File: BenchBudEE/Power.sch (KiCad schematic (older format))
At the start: 11 parts

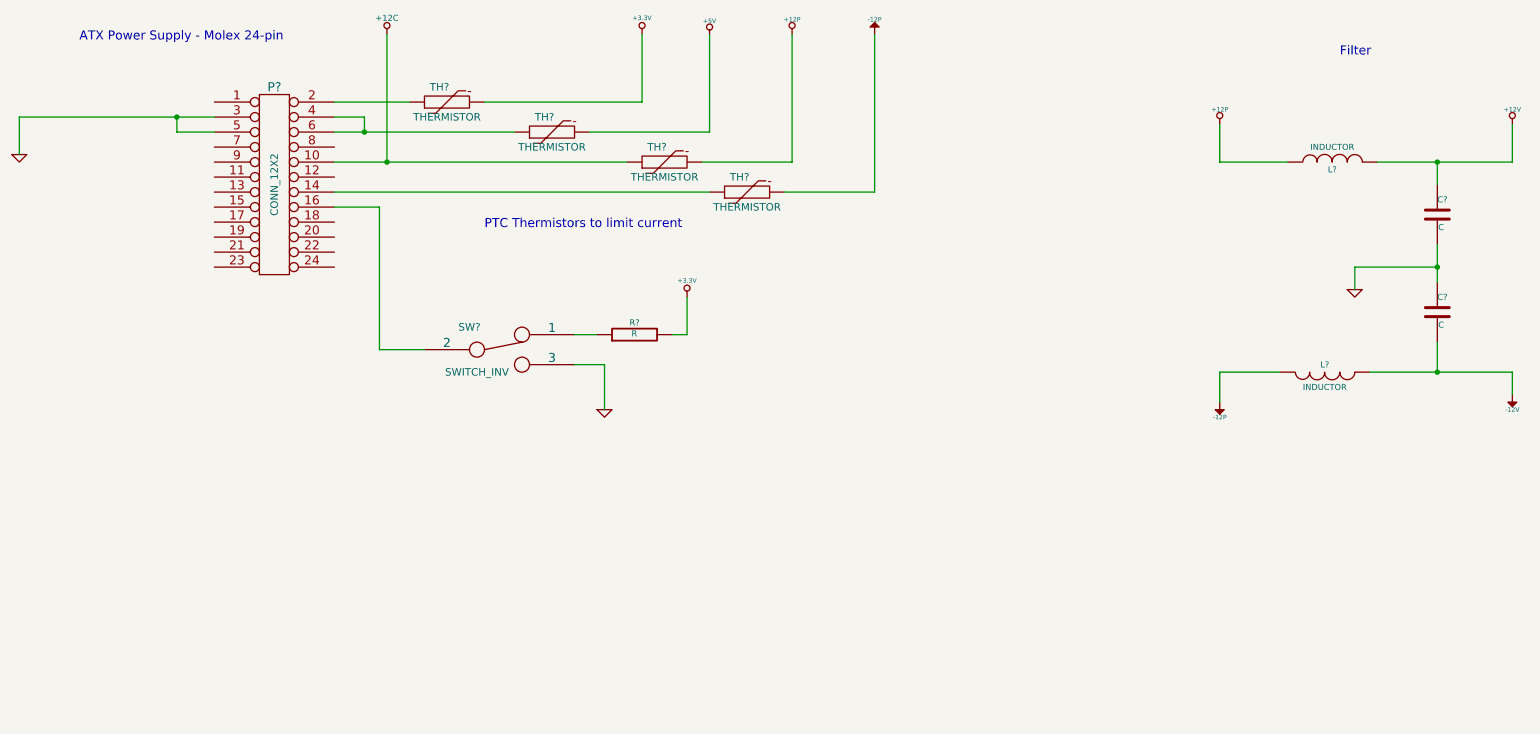
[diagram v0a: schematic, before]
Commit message: Connected Arduino power/ground. +5V power filtering. Removed current monitoring.
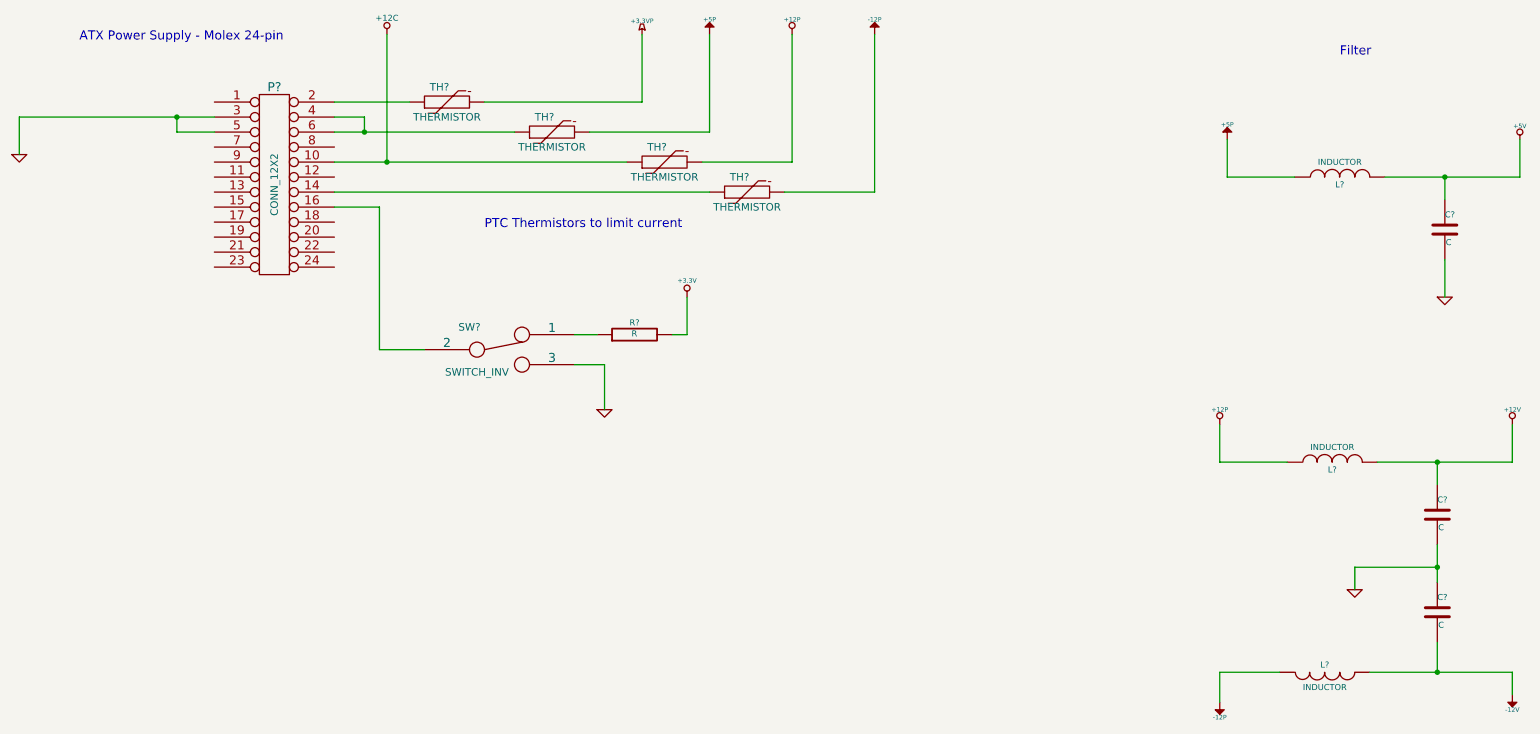
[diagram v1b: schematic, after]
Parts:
- added C?: C, ~, symbol C
- added L?: INDUCTOR, ~, symbol INDUCTOR
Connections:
- net +3.3V: no longer TH?.2
- net +5V: now also C?.1, L?.2; no longer TH?.2
- net GND: now also C?.2
- new net +3.3VP: TH?.2
- new net +5P: L?.1, TH?.2
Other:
- moved on the sheet: C?, L?
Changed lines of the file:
@@
 Sheet 4 9
 Title ""
-Date "14 feb 2014"
+Date "19 feb 2014"
 Rev ""
 Comp ""
@@
 Connection ~ 3150 1700
 Wire Wire Line
-	2150 1600 850  1600
+	850  1600 2150 1600
 Wire Wire Line
 	2150 1700 1900 1700
@@
 Text Notes 1250 1100 0    60   ~ 0
 ATX Power Supply - Molex 24-pin
-Connection ~ 10300 1900
-Wire Wire Line
-	10800 1900 10800 1650
+Connection ~ 10300 3900
+Wire Wire Line
+	10800 3900 10800 3650
 $Comp
 L +12V #PWR?
 U 1 1 52F6355D
-P 10800 1650
-F 0 "#PWR?" H 10800 1600 20  0001 C CNN
-F 1 "+12V" H 10800 1750 30  0000 C CNN
-F 2 "" H 10800 1650 60  0000 C CNN
-F 3 "" H 10800 1650 60  0000 C CNN
-	1    10800 1650
-	1    0    0    -1
-$EndComp
-Connection ~ 10300 3300
-Wire Wire Line
-	10800 3300 10800 3450
+P 10800 3650
+F 0 "#PWR?" H 10800 3600 20  0001 C CNN
+F 1 "+12V" H 10800 3750 30  0000 C CNN
+F 2 "" H 10800 3650 60  0000 C CNN
+F 3 "" H 10800 3650 60  0000 C CNN
+	1    10800 3650
+	1    0    0    -1
+$EndComp
+Connection ~ 10300 5300
+Wire Wire Line
+	10800 5300 10800 5450
 $Comp
 L -12V #PWR?
 U 1 1 52F63518
-P 10800 3450
-F 0 "#PWR?" H 10800 3580 20  0001 C CNN
-F 1 "-12V" H 10800 3550 30  0000 C CNN
-F 2 "" H 10800 3450 60  0000 C CNN
-F 3 "" H 10800 3450 60  0000 C CNN
-	1    10800 3450
+P 10800 5450
+F 0 "#PWR?" H 10800 5580 20  0001 C CNN
+F 1 "-12V" H 10800 5550 30  0000 C CNN
+F 2 "" H 10800 5450 60  0000 C CNN
+F 3 "" H 10800 5450 60  0000 C CNN
+	1    10800 5450
 	1    0    0    1
 $EndComp
-Connection ~ 10300 2600
-Wire Wire Line
-	9750 2600 10300 2600
-Wire Wire Line
-	9750 2750 9750 2600
-Wire Wire Line
-	8850 1900 8850 1650
-Wire Wire Line
-	9300 1900 8850 1900
-Wire Wire Line
-	9900 1900 10800 1900
-Wire Wire Line
-	10300 2050 10300 1900
-Wire Wire Line
-	10300 2700 10300 2450
-Wire Wire Line
-	10300 3300 10300 3100
-Wire Wire Line
-	9850 3300 10800 3300
-Wire Wire Line
-	8850 3300 9250 3300
-Wire Wire Line
-	8850 3500 8850 3300
+Connection ~ 10300 4600
+Wire Wire Line
+	9750 4600 10300 4600
+Wire Wire Line
+	9750 4750 9750 4600
+Wire Wire Line
+	8850 3900 8850 3650
+Wire Wire Line
+	9300 3900 8850 3900
+Wire Wire Line
+	9900 3900 10800 3900
+Wire Wire Line
+	10300 4050 10300 3900
+Wire Wire Line
+	10300 4450 10300 4700
+Wire Wire Line
+	10300 5300 10300 5100
+Wire Wire Line
+	9850 5300 10800 5300
+Wire Wire Line
+	8850 5300 9250 5300
+Wire Wire Line
+	8850 5500 8850 5300
 $Comp
 L C C?
 U 1 1 52F6342F
-P 10300 2250
-F 0 "C?" H 10300 2350 40  0000 L CNN
-F 1 "C" H 10306 2165 40  0000 L CNN
-F 2 "~" H 10338 2100 30  0000 C CNN
-F 3 "~" H 10300 2250 60  0000 C CNN
-	1    10300 2250
+P 10300 4250
+F 0 "C?" H 10300 4350 40  0000 L CNN
+F 1 "C" H 10306 4165 40  0000 L CNN
+F 2 "~" H 10338 4100 30  0000 C CNN
+F 3 "~" H 10300 4250 60  0000 C CNN
+	1    10300 4250
 	1    0    0    -1
 $EndComp
@@
 L C C?
 U 1 1 52F63418
-P 10300 2900
-F 0 "C?" H 10300 3000 40  0000 L CNN
-F 1 "C" H 10306 2815 40  0000 L CNN
-F 2 "~" H 10338 2750 30  0000 C CNN
-F 3 "~" H 10300 2900 60  0000 C CNN
-	1    10300 2900
+P 10300 4900
+F 0 "C?" H 10300 5000 40  0000 L CNN
+F 1 "C" H 10306 4815 40  0000 L CNN
+F 2 "~" H 10338 4750 30  0000 C CNN
+F 3 "~" H 10300 4900 60  0000 C CNN
+	1    10300 4900
 	1    0    0    -1
 $EndComp
@@
 L INDUCTOR L?
 U 1 1 52F63410
-P 9550 3300
-F 0 "L?" V 9500 3300 40  0000 C CNN
-F 1 "INDUCTOR" V 9650 3300 40  0000 C CNN
-F 2 "~" H 9550 3300 60  0000 C CNN
-F 3 "~" H 9550 3300 60  0000 C CNN
-	1    9550 3300
+P 9550 5300
+F 0 "L?" V 9500 5300 40  0000 C CNN
+F 1 "INDUCTOR" V 9650 5300 40  0000 C CNN
+F 2 "~" H 9550 5300 60  0000 C CNN
+F 3 "~" H 9550 5300 60  0000 C CNN
+	1    9550 5300
 	0    -1   1    0
 $EndComp
@@
 L INDUCTOR L?
 U 1 1 52F633F9
-P 9600 1900
-F 0 "L?" V 9550 1900 40  0000 C CNN
-F 1 "INDUCTOR" V 9700 1900 40  0000 C CNN
-F 2 "~" H 9600 1900 60  0000 C CNN
-F 3 "~" H 9600 1900 60  0000 C CNN
-	1    9600 1900
+P 9600 3900
+F 0 "L?" V 9550 3900 40  0000 C CNN
+F 1 "INDUCTOR" V 9700 3900 40  0000 C CNN
+F 2 "~" H 9600 3900 60  0000 C CNN
+F 3 "~" H 9600 3900 60  0000 C CNN
+	1    9600 3900
 	0    -1   -1   0
 $EndComp
@@
 L GND #PWR?
 U 1 1 52F633F1
-P 9750 2750
-F 0 "#PWR?" H 9750 2750 30  0001 C CNN
-F 1 "GND" H 9750 2680 30  0001 C CNN
-F 2 "" H 9750 2750 60  0000 C CNN
-F 3 "" H 9750 2750 60  0000 C CNN
-	1    9750 2750
+P 9750 4750
+F 0 "#PWR?" H 9750 4750 30  0001 C CNN
+F 1 "GND" H 9750 4680 30  0001 C CNN
+F 2 "" H 9750 4750 60  0000 C CNN
+F 3 "" H 9750 4750 60  0000 C CNN
+	1    9750 4750
 	1    0    0    -1
 $EndComp
@@
 L -12P #PWR?
 U 1 1 52F633EB
-P 8850 3500
-F 0 "#PWR?" H 8850 3630 20  0001 C CNN
-F 1 "-12P" H 8850 3600 30  0000 C CNN
-F 2 "" H 8850 3500 60  0000 C CNN
-F 3 "" H 8850 3500 60  0000 C CNN
-	1    8850 3500
+P 8850 5500
+F 0 "#PWR?" H 8850 5630 20  0001 C CNN
+F 1 "-12P" H 8850 5600 30  0000 C CNN
+F 2 "" H 8850 5500 60  0000 C CNN
+F 3 "" H 8850 5500 60  0000 C CNN
+	1    8850 5500
 	1    0    0    1
 $EndComp
@@
 L +12P #PWR?
 U 1 1 52F633E5
-P 8850 1650
-F 0 "#PWR?" H 8850 1620 30  0001 C CNN
-F 1 "+12P" H 8850 1750 30  0000 C CNN
-F 2 "" H 8850 1650 60  0000 C CNN
-F 3 "" H 8850 1650 60  0000 C CNN
-	1    8850 1650
+P 8850 3650
+F 0 "#PWR?" H 8850 3620 30  0001 C CNN
+F 1 "+12P" H 8850 3750 30  0000 C CNN
+F 2 "" H 8850 3650 60  0000 C CNN
+F 3 "" H 8850 3650 60  0000 C CNN
+	1    8850 3650
 	1    0    0    -1
 $EndComp
@@
 	1    0    0    -1
 $EndComp
-$Comp
-L +5V #PWR?
-U 1 1 52F62810
-P 5450 1050
-F 0 "#PWR?" H 5450 1140 20  0001 C CNN
-F 1 "+5V" H 5450 1140 30  0000 C CNN
-F 2 "" H 5450 1050 60  0000 C CNN
-F 3 "" H 5450 1050 60  0000 C CNN
-	1    5450 1050
-	1    0    0    -1
-$EndComp
-$Comp
-L +3.3V #PWR?
-U 1 1 52F627FA
-P 5000 1050
-F 0 "#PWR?" H 5000 1010 30  0001 C CNN
-F 1 "+3.3V" H 5000 1160 30  0000 C CNN
-F 2 "" H 5000 1050 60  0000 C CNN
-F 3 "" H 5000 1050 60  0000 C CNN
-	1    5000 1050
-	1    0    0    -1
-$EndComp
 Wire Wire Line
 	3300 1900 3300 1050
@@
 	0    -1   -1   0
 $EndComp
+Connection ~ 10350 2000
+Wire Wire Line
+	10850 2000 10850 1750
+Wire Wire Line
+	8900 2000 8900 1750
+Wire Wire Line
+	9350 2000 8900 2000
+Wire Wire Line
+	9950 2000 10850 2000
+Wire Wire Line
+	10350 2150 10350 2000
+$Comp
+L C C?
+U 1 1 53041CC8
+P 10350 2350
+F 0 "C?" H 10350 2450 40  0000 L CNN
+F 1 "C" H 10356 2265 40  0000 L CNN
+F 2 "~" H 10388 2200 30  0000 C CNN
+F 3 "~" H 10350 2350 60  0000 C CNN
+	1    10350 2350
+	1    0    0    -1
+$EndComp
+$Comp
+L INDUCTOR L?
+U 1 1 53041CCE
+P 9650 2000
+F 0 "L?" V 9600 2000 40  0000 C CNN
+F 1 "INDUCTOR" V 9750 2000 40  0000 C CNN
+F 2 "~" H 9650 2000 60  0000 C CNN
+F 3 "~" H 9650 2000 60  0000 C CNN
+	1    9650 2000
+	0    -1   -1   0
+$EndComp
+Wire Wire Line
+	10350 2550 10350 2800
+$Comp
+L GND #PWR?
+U 1 1 53041D20
+P 10350 2800
+F 0 "#PWR?" H 10350 2800 30  0001 C CNN
+F 1 "GND" H 10350 2730 30  0001 C CNN
+F 2 "" H 10350 2800 60  0000 C CNN
+F 3 "" H 10350 2800 60  0000 C CNN
+	1    10350 2800
+	1    0    0    -1
+$EndComp
+$Comp
+L +5P #PWR?
+U 1 1 53041F77
+P 5450 1050
+F 0 "#PWR?" H 5450 1180 20  0001 C CNN
+F 1 "+5P" H 5450 1150 30  0000 C CNN
+F 2 "" H 5450 1050 60  0000 C CNN
+F 3 "" H 5450 1050 60  0000 C CNN
+	1    5450 1050
+	1    0    0    -1
+$EndComp
+$Comp
+L +5P #PWR?
+U 1 1 53041F84
+P 8900 1750
+F 0 "#PWR?" H 8900 1880 20  0001 C CNN
+F 1 "+5P" H 8900 1850 30  0000 C CNN
+F 2 "" H 8900 1750 60  0000 C CNN
+F 3 "" H 8900 1750 60  0000 C CNN
+	1    8900 1750
+	1    0    0    -1
+$EndComp
+$Comp
+L +3.3VP #PWR?
+U 1 1 530421E7
+P 5000 1050
+F 0 "#PWR?" H 5050 1080 20  0001 C CNN
+F 1 "+3.3VP" H 5000 1140 30  0000 C CNN
+F 2 "" H 5000 1050 60  0000 C CNN
+F 3 "" H 5000 1050 60  0000 C CNN
+	1    5000 1050
+	1    0    0    -1
+$EndComp
+$Comp
+L +5V #PWR?
+U 1 1 530426C4
+P 10850 1750
+F 0 "#PWR?" H 10850 1840 20  0001 C CNN
+F 1 "+5V" H 10850 1840 30  0000 C CNN
+F 2 "" H 10850 1750 60  0000 C CNN
+F 3 "" H 10850 1750 60  0000 C CNN
+	1    10850 1750
+	1    0    0    -1
+$EndComp
 $EndSCHEMATC

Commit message: Placed the relay components.
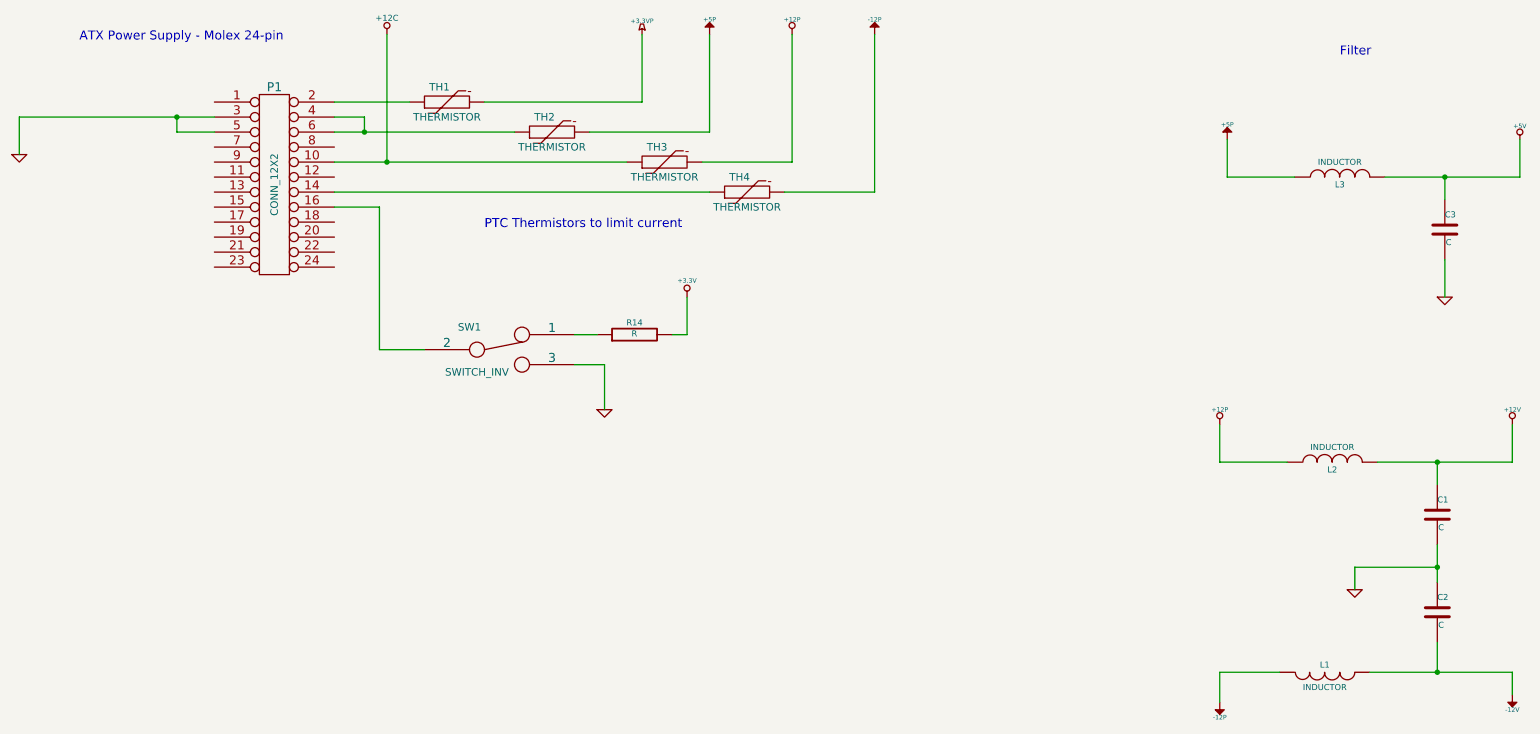
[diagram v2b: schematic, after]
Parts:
- gave numbers to parts that had none: 13
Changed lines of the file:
@@
 Sheet 4 9
 Title ""
-Date "19 feb 2014"
+Date "20 feb 2014"
 Rev ""
 Comp ""
@@
 $EndDescr
 $Comp
-L CONN_12X2 P?
+L CONN_12X2 P1
 U 1 1 52F627D0
 P 2550 2050
-F 0 "P?" H 2550 2700 60  0000 C CNN
+F 0 "P1" H 2550 2700 60  0000 C CNN
 F 1 "CONN_12X2" V 2550 2050 50  0000 C CNN
 F 2 "" H 2550 2050 60  0000 C CNN
@@
 	850  1600 850  1850
 $Comp
-L GND #PWR?
+L GND #PWR13
 U 1 1 52F627E6
 P 850 1850
-F 0 "#PWR?" H 850 1850 30  0001 C CNN
+F 0 "#PWR13" H 850 1850 30  0001 C CNN
 F 1 "GND" H 850 1780 30  0001 C CNN
 F 2 "" H 850 1850 60  0000 C CNN
@@
 	10800 3900 10800 3650
 $Comp
-L +12V #PWR?
+L +12V #PWR26
 U 1 1 52F6355D
 P 10800 3650
-F 0 "#PWR?" H 10800 3600 20  0001 C CNN
+F 0 "#PWR26" H 10800 3600 20  0001 C CNN
 F 1 "+12V" H 10800 3750 30  0000 C CNN
 F 2 "" H 10800 3650 60  0000 C CNN
@@
 	10800 5300 10800 5450
 $Comp
-L -12V #PWR?
+L -12V #PWR27
 U 1 1 52F63518
 P 10800 5450
-F 0 "#PWR?" H 10800 5580 20  0001 C CNN
+F 0 "#PWR27" H 10800 5580 20  0001 C CNN
 F 1 "-12V" H 10800 5550 30  0000 C CNN
 F 2 "" H 10800 5450 60  0000 C CNN
@@
 	8850 5500 8850 5300
 $Comp
-L C C?
+L C C1
 U 1 1 52F6342F
 P 10300 4250
-F 0 "C?" H 10300 4350 40  0000 L CNN
+F 0 "C1" H 10300 4350 40  0000 L CNN
 F 1 "C" H 10306 4165 40  0000 L CNN
 F 2 "~" H 10338 4100 30  0000 C CNN
@@
 $EndComp
 $Comp
-L C C?
+L C C2
 U 1 1 52F63418
 P 10300 4900
-F 0 "C?" H 10300 5000 40  0000 L CNN
+F 0 "C2" H 10300 5000 40  0000 L CNN
 F 1 "C" H 10306 4815 40  0000 L CNN
 F 2 "~" H 10338 4750 30  0000 C CNN
@@
 $EndComp
 $Comp
-L INDUCTOR L?
+L INDUCTOR L1
 U 1 1 52F63410
 P 9550 5300
-F 0 "L?" V 9500 5300 40  0000 C CNN
+F 0 "L1" V 9500 5300 40  0000 C CNN
 F 1 "INDUCTOR" V 9650 5300 40  0000 C CNN
 F 2 "~" H 9550 5300 60  0000 C CNN
@@
 $EndComp
 $Comp
-L INDUCTOR L?
+L INDUCTOR L2
 U 1 1 52F633F9
 P 9600 3900
-F 0 "L?" V 9550 3900 40  0000 C CNN
+F 0 "L2" V 9550 3900 40  0000 C CNN
 F 1 "INDUCTOR" V 9700 3900 40  0000 C CNN
 F 2 "~" H 9600 3900 60  0000 C CNN
@@
 PTC Thermistors to limit current
 $Comp
-L GND #PWR?
+L GND #PWR24
 U 1 1 52F633F1
 P 9750 4750
-F 0 "#PWR?" H 9750 4750 30  0001 C CNN
+F 0 "#PWR24" H 9750 4750 30  0001 C CNN
 F 1 "GND" H 9750 4680 30  0001 C CNN
 F 2 "" H 9750 4750 60  0000 C CNN
@@
 $EndComp
 $Comp
-L -12P #PWR?
+L -12P #PWR22
 U 1 1 52F633EB
 P 8850 5500
-F 0 "#PWR?" H 8850 5630 20  0001 C CNN
+F 0 "#PWR22" H 8850 5630 20  0001 C CNN
 F 1 "-12P" H 8850 5600 30  0000 C CNN
 F 2 "" H 8850 5500 60  0000 C CNN
@@
 $EndComp
 $Comp
-L +12P #PWR?
+L +12P #PWR21
 U 1 1 52F633E5
 P 8850 3650
-F 0 "#PWR?" H 8850 3620 30  0001 C CNN
+F 0 "#PWR21" H 8850 3620 30  0001 C CNN
 F 1 "+12P" H 8850 3750 30  0000 C CNN
 F 2 "" H 8850 3650 60  0000 C CNN
@@
 	5200 3050 5300 3050
 $Comp
-L +3.3V #PWR?
+L +3.3V #PWR17
 U 1 1 52F6321F
 P 5300 2800
-F 0 "#PWR?" H 5300 2760 30  0001 C CNN
+F 0 "#PWR17" H 5300 2760 30  0001 C CNN
 F 1 "+3.3V" H 5300 2910 30  0000 C CNN
 F 2 "" H 5300 2800 60  0000 C CNN
@@
 	4550 3050 4700 3050
 $Comp
-L R R?
+L R R14
 U 1 1 52F631F6
 P 4950 3050
-F 0 "R?" V 5030 3050 40  0000 C CNN
+F 0 "R14" V 5030 3050 40  0000 C CNN
 F 1 "R" V 4957 3051 40  0000 C CNN
 F 2 "~" V 4880 3050 30  0000 C CNN
@@
 	4550 3250 4750 3250
 $Comp
-L GND #PWR?
+L GND #PWR15
 U 1 1 52F631D4
 P 4750 3550
-F 0 "#PWR?" H 4750 3550 30  0001 C CNN
+F 0 "#PWR15" H 4750 3550 30  0001 C CNN
 F 1 "GND" H 4750 3480 30  0001 C CNN
 F 2 "" H 4750 3550 60  0000 C CNN
@@
 	5400 1900 6000 1900
 $Comp
-L -12P #PWR?
+L -12P #PWR20
 U 1 1 52F62FBB
 P 6550 1050
-F 0 "#PWR?" H 6550 1180 20  0001 C CNN
+F 0 "#PWR20" H 6550 1180 20  0001 C CNN
 F 1 "-12P" H 6550 1150 30  0000 C CNN
 F 2 "" H 6550 1050 60  0000 C CNN
@@
 $EndComp
 $Comp
-L +12P #PWR?
+L +12P #PWR19
 U 1 1 52F62A76
 P 6000 1050
-F 0 "#PWR?" H 6000 1020 30  0001 C CNN
+F 0 "#PWR19" H 6000 1020 30  0001 C CNN
 F 1 "+12P" H 6000 1150 30  0000 C CNN
 F 2 "" H 6000 1050 60  0000 C CNN
@@
 	3950 1500 5000 1500
 $Comp
-L SWITCH_INV SW?
+L SWITCH_INV SW1
 U 1 1 52F629F1
 P 4050 3150
-F 0 "SW?" H 3850 3300 50  0000 C CNN
+F 0 "SW1" H 3850 3300 50  0000 C CNN
 F 1 "SWITCH_INV" H 3900 3000 50  0000 C CNN
 F 2 "~" H 4050 3150 60  0000 C CNN
@@
 Connection ~ 3300 1900
 $Comp
-L +12C #PWR?
+L +12C #PWR14
 U 1 1 52FAE7F5
 P 3300 1050
-F 0 "#PWR?" H 3300 1020 30  0001 C CNN
+F 0 "#PWR14" H 3300 1020 30  0001 C CNN
 F 1 "+12C" H 3300 1160 40  0000 C CNN
 F 2 "" H 3300 1050 60  0000 C CNN
@@
 $EndComp
 $Comp
-L THERMISTOR TH?
+L THERMISTOR TH1
 U 1 1 52FB015D
 P 3700 1500
-F 0 "TH?" V 3800 1550 50  0000 C CNN
+F 0 "TH1" V 3800 1550 50  0000 C CNN
 F 1 "THERMISTOR" V 3600 1500 50  0000 C CNN
 F 2 "~" H 3700 1500 60  0000 C CNN
@@
 $EndComp
 $Comp
-L THERMISTOR TH?
+L THERMISTOR TH2
 U 1 1 52FB016A
 P 4400 1700
-F 0 "TH?" V 4500 1750 50  0000 C CNN
+F 0 "TH2" V 4500 1750 50  0000 C CNN
 F 1 "THERMISTOR" V 4300 1700 50  0000 C CNN
 F 2 "~" H 4400 1700 60  0000 C CNN
@@
 $EndComp
 $Comp
-L THERMISTOR TH?
+L THERMISTOR TH3
 U 1 1 52FB0170
 P 5150 1900
-F 0 "TH?" V 5250 1950 50  0000 C CNN
+F 0 "TH3" V 5250 1950 50  0000 C CNN
 F 1 "THERMISTOR" V 5050 1900 50  0000 C CNN
 F 2 "~" H 5150 1900 60  0000 C CNN
@@
 $EndComp
 $Comp
-L THERMISTOR TH?
+L THERMISTOR TH4
 U 1 1 52FB0180
 P 5700 2100
-F 0 "TH?" V 5800 2150 50  0000 C CNN
+F 0 "TH4" V 5800 2150 50  0000 C CNN
 F 1 "THERMISTOR" V 5600 2100 50  0000 C CNN
 F 2 "~" H 5700 2100 60  0000 C CNN
@@
 	10350 2150 10350 2000
 $Comp
-L C C?
+L C C3
 U 1 1 53041CC8
 P 10350 2350
-F 0 "C?" H 10350 2450 40  0000 L CNN
+F 0 "C3" H 10350 2450 40  0000 L CNN
 F 1 "C" H 10356 2265 40  0000 L CNN
 F 2 "~" H 10388 2200 30  0000 C CNN
@@
 $EndComp
 $Comp
-L INDUCTOR L?
+L INDUCTOR L3
 U 1 1 53041CCE
 P 9650 2000
-F 0 "L?" V 9600 2000 40  0000 C CNN
+F 0 "L3" V 9600 2000 40  0000 C CNN
 F 1 "INDUCTOR" V 9750 2000 40  0000 C CNN
 F 2 "~" H 9650 2000 60  0000 C CNN
@@
 	10350 2550 10350 2800
 $Comp
-L GND #PWR?
+L GND #PWR25
 U 1 1 53041D20
 P 10350 2800
-F 0 "#PWR?" H 10350 2800 30  0001 C CNN
+F 0 "#PWR25" H 10350 2800 30  0001 C CNN
 F 1 "GND" H 10350 2730 30  0001 C CNN
 F 2 "" H 10350 2800 60  0000 C CNN
@@
 $EndComp
 $Comp
-L +5P #PWR?
+L +5P #PWR18
 U 1 1 53041F77
 P 5450 1050
-F 0 "#PWR?" H 5450 1180 20  0001 C CNN
+F 0 "#PWR18" H 5450 1180 20  0001 C CNN
 F 1 "+5P" H 5450 1150 30  0000 C CNN
 F 2 "" H 5450 1050 60  0000 C CNN
@@
 $EndComp
 $Comp
-L +5P #PWR?
+L +5P #PWR23
 U 1 1 53041F84
 P 8900 1750
-F 0 "#PWR?" H 8900 1880 20  0001 C CNN
+F 0 "#PWR23" H 8900 1880 20  0001 C CNN
 F 1 "+5P" H 8900 1850 30  0000 C CNN
 F 2 "" H 8900 1750 60  0000 C CNN
@@
 $EndComp
 $Comp
-L +3.3VP #PWR?
+L +3.3VP #PWR16
 U 1 1 530421E7
 P 5000 1050
-F 0 "#PWR?" H 5050 1080 20  0001 C CNN
+F 0 "#PWR16" H 5050 1080 20  0001 C CNN
 F 1 "+3.3VP" H 5000 1140 30  0000 C CNN
 F 2 "" H 5000 1050 60  0000 C CNN
@@
 $EndComp
 $Comp
-L +5V #PWR?
+L +5V #PWR28
 U 1 1 530426C4
 P 10850 1750
-F 0 "#PWR?" H 10850 1840 20  0001 C CNN
+F 0 "#PWR28" H 10850 1840 20  0001 C CNN
 F 1 "+5V" H 10850 1840 30  0000 C CNN
 F 2 "" H 10850 1750 60  0000 C CNN
